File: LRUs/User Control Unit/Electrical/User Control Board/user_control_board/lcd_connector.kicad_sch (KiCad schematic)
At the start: 1 part

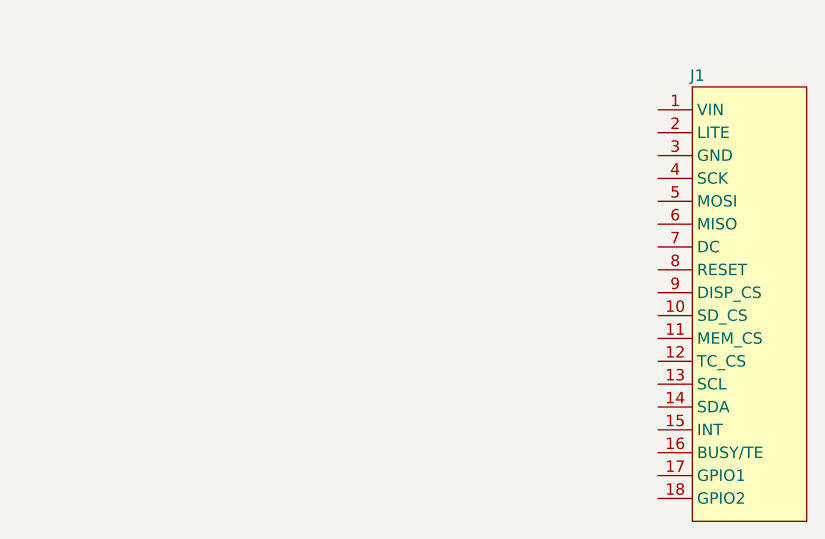
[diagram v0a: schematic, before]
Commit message: PICO partial wiring to -> (EYESPI, RFM transceiver).  Mosfet partially wired.
Don't know how to do the SD card XD.
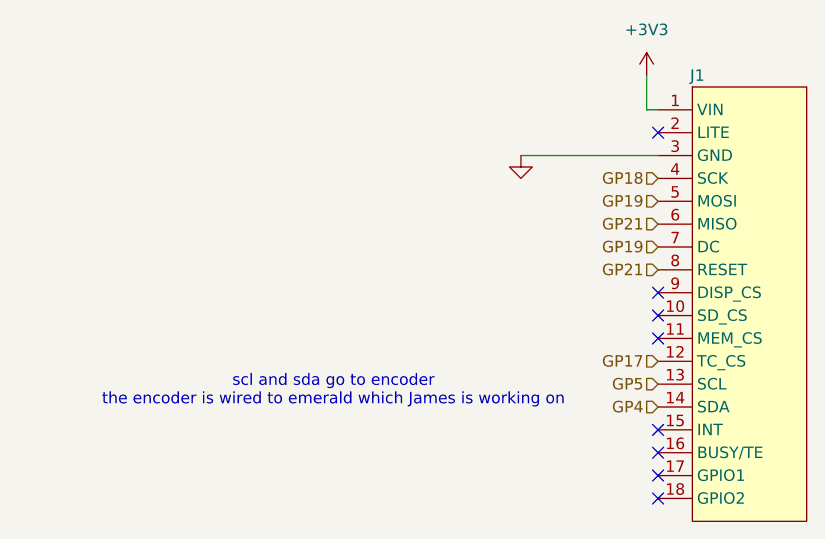
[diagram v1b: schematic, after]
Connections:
- net +3V3: now reaches J1.1 (VIN)
- net GP17: now reaches J1.12 (TC_CS)
- net GP5: now reaches J1.13 (SCL)
- net GP4: now reaches J1.14 (SDA)
- net GND: now reaches J1.3 (GND)
- net GP18: now reaches J1.4 (SCK)
- net GP19: now reaches J1.5 (MOSI)
- net GP19: now also J1.7 (DC)
- net GP21: now reaches J1.6 (MISO)
- net GP21: now also J1.8 (RESET)
- no-connect marks 0 -> 8
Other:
- note added: "scl and sda go to encoder the encoder is wired to emerald which James is working on"

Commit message: need to run DCR
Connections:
- net GP19: no longer J1.7 (DC)
- net GP21: no longer J1.6 (MISO)
- new net GP16: J1.6 (MISO)
- new net GP20: J1.7 (DC)
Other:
- note removed: "scl and sda go to encoder the encoder is wired to emerald which James is working on"
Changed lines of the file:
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@@
 	(generator_version "10.0")
 	(paper "A4")
-	(text "scl and sda go to encoder\nthe encoder is wired to emerald which James is working on"
-		(exclude_from_sim no)
-		(at 162.052 106.172 0)
-		(effects
-			(font
-				(size 1.27 1.27)
-			)
-		)
-	)
 	(no_connect
 		(at 198.12 113.03)
@@
 		)
 	)
-	(hierarchical_label "GP21"
+	(global_label "GP20"
+		(shape input)
+		(at 198.12 90.17 180)
+		(fields_autoplaced yes)
+		(effects
+			(font
+				(size 1.27 1.27)
+			)
+			(justify right)
+		)
+		(property "Intersheetrefs" "${INTERSHEET_REFS}"
+			(at 190.1758 90.17 0)
+			(hide yes)
+			(show_name no)
+			(do_not_autoplace no)
+			(effects
+				(font
+					(size 1.27 1.27)
+				)
+				(justify right)
+			)
+		)
+	)
+	(global_label "GP5"
+		(shape input)
+		(at 198.12 105.41 180)
+		(fields_autoplaced yes)
+		(effects
+			(font
+				(size 1.27 1.27)
+			)
+			(justify right)
+		)
+		(property "Intersheetrefs" "${INTERSHEET_REFS}"
+			(at 191.3853 105.41 0)
+			(hide yes)
+			(show_name no)
+			(do_not_autoplace no)
+			(effects
+				(font
+					(size 1.27 1.27)
+				)
+				(justify right)
+			)
+		)
+	)
+	(global_label "GP18"
+		(shape input)
+		(at 198.12 82.55 180)
+		(fields_autoplaced yes)
+		(effects
+			(font
+				(size 1.27 1.27)
+			)
+			(justify right)
+		)
+		(property "Intersheetrefs" "${INTERSHEET_REFS}"
+			(at 190.1758 82.55 0)
+			(hide yes)
+			(show_name no)
+			(do_not_autoplace no)
+			(effects
+				(font
+					(size 1.27 1.27)
+				)
+				(justify right)
+			)
+		)
+	)
+	(global_label "GP21"
+		(shape input)
+		(at 198.12 92.71 180)
+		(fields_autoplaced yes)
+		(effects
+			(font
+				(size 1.27 1.27)
+			)
+			(justify right)
+		)
+		(property "Intersheetrefs" "${INTERSHEET_REFS}"
+			(at 190.1758 92.71 0)
+			(hide yes)
+			(show_name no)
+			(do_not_autoplace no)
+			(effects
+				(font
+					(size 1.27 1.27)
+				)
+				(justify right)
+			)
+		)
+	)
+	(global_label "GP4"
+		(shape input)
+		(at 198.12 107.95 180)
+		(fields_autoplaced yes)
+		(effects
+			(font
+				(size 1.27 1.27)
+			)
+			(justify right)
+		)
+		(property "Intersheetrefs" "${INTERSHEET_REFS}"
+			(at 191.3853 107.95 0)
+			(hide yes)
+			(show_name no)
+			(do_not_autoplace no)
+			(effects
+				(font
+					(size 1.27 1.27)
+				)
+				(justify right)
+			)
+		)
+	)
+	(global_label "GP17"
+		(shape input)
+		(at 198.12 102.87 180)
+		(fields_autoplaced yes)
+		(effects
+			(font
+				(size 1.27 1.27)
+			)
+			(justify right)
+		)
+		(property "Intersheetrefs" "${INTERSHEET_REFS}"
+			(at 190.1758 102.87 0)
+			(hide yes)
+			(show_name no)
+			(do_not_autoplace no)
+			(effects
+				(font
+					(size 1.27 1.27)
+				)
+				(justify right)
+			)
+		)
+	)
+	(global_label "GP16"
 		(shape input)
 		(at 198.12 87.63 180)
-		(effects
-			(font
-				(size 1.27 1.27)
-			)
-			(justify right)
-		)
-	)
-	(hierarchical_label "GP21"
-		(shape input)
-		(at 198.12 92.71 180)
-		(effects
-			(font
-				(size 1.27 1.27)
-			)
-			(justify right)
-		)
-	)
-	(hierarchical_label "GP19"
+		(fields_autoplaced yes)
+		(effects
+			(font
+				(size 1.27 1.27)
+			)
+			(justify right)
+		)
+		(property "Intersheetrefs" "${INTERSHEET_REFS}"
+			(at 190.1758 87.63 0)
+			(hide yes)
+			(show_name no)
+			(do_not_autoplace no)
+			(effects
+				(font
+					(size 1.27 1.27)
+				)
+				(justify right)
+			)
+		)
+	)
+	(global_label "GP19"
 		(shape input)
 		(at 198.12 85.09 180)
-		(effects
-			(font
-				(size 1.27 1.27)
-			)
-			(justify right)
-		)
-	)
-	(hierarchical_label "GP19"
-		(shape input)
-		(at 198.12 90.17 180)
-		(effects
-			(font
-				(size 1.27 1.27)
-			)
-			(justify right)
-		)
-	)
-	(hierarchical_label "GP5"
-		(shape input)
-		(at 198.12 105.41 180)
-		(effects
-			(font
-				(size 1.27 1.27)
-			)
-			(justify right)
-		)
-	)
-	(hierarchical_label "GP18"
-		(shape input)
-		(at 198.12 82.55 180)
-		(effects
-			(font
-				(size 1.27 1.27)
-			)
-			(justify right)
-		)
-	)
-	(hierarchical_label "GP4"
-		(shape input)
-		(at 198.12 107.95 180)
-		(effects
-			(font
-				(size 1.27 1.27)
-			)
-			(justify right)
-		)
-	)
-	(hierarchical_label "GP17"
-		(shape input)
-		(at 198.12 102.87 180)
-		(effects
-			(font
-				(size 1.27 1.27)
-			)
-			(justify right)
-		)
-	)
+		(fields_autoplaced yes)
+		(effects
+			(font
+				(size 1.27 1.27)
+			)
+			(justify right)
+		)
+		(property "Intersheetrefs" "${INTERSHEET_REFS}"
+			(at 190.1758 85.09 0)
+			(hide yes)
+			(show_name no)
+			(do_not_autoplace no)
+			(effects
+				(font
+					(size 1.27 1.27)
+				)
+				(justify right)
+			)
+		)
+	)

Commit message: connectors and 5v buck partially done
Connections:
- net GP16 renamed RADIO_CS
- net GP17 renamed LCD_CS
- net GP18 renamed SCK
- net GP19 renamed MOSI
- net GP20 renamed LCD_DC
- net GP21 renamed LCD_RESET
- net GP4 renamed I2C0_SDA
- net GP5 renamed I2C0_SCL
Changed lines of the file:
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@@
 		)
 	)
-	(global_label "GP20"
+	(global_label "LCD_DC"
 		(shape input)
 		(at 198.12 90.17 180)
@@
 		)
 		(property "Intersheetrefs" "${INTERSHEET_REFS}"
-			(at 190.1758 90.17 0)
-			(hide yes)
-			(show_name no)
-			(do_not_autoplace no)
-			(effects
-				(font
-					(size 1.27 1.27)
-				)
-				(justify right)
-			)
-		)
-	)
-	(global_label "GP5"
+			(at 188.0591 90.17 0)
+			(hide yes)
+			(show_name no)
+			(do_not_autoplace no)
+			(effects
+				(font
+					(size 1.27 1.27)
+				)
+				(justify right)
+			)
+		)
+	)
+	(global_label "I2C0_SDA"
+		(shape input)
+		(at 198.12 107.95 180)
+		(fields_autoplaced yes)
+		(effects
+			(font
+				(size 1.27 1.27)
+			)
+			(justify right)
+		)
+		(property "Intersheetrefs" "${INTERSHEET_REFS}"
+			(at 186.3053 107.95 0)
+			(hide yes)
+			(show_name no)
+			(do_not_autoplace no)
+			(effects
+				(font
+					(size 1.27 1.27)
+				)
+				(justify right)
+			)
+		)
+	)
+	(global_label "SCK"
+		(shape input)
+		(at 198.12 82.55 180)
+		(fields_autoplaced yes)
+		(effects
+			(font
+				(size 1.27 1.27)
+			)
+			(justify right)
+		)
+		(property "Intersheetrefs" "${INTERSHEET_REFS}"
+			(at 191.3853 82.55 0)
+			(hide yes)
+			(show_name no)
+			(do_not_autoplace no)
+			(effects
+				(font
+					(size 1.27 1.27)
+				)
+				(justify right)
+			)
+		)
+	)
+	(global_label "LCD_RESET"
+		(shape input)
+		(at 198.12 92.71 180)
+		(fields_autoplaced yes)
+		(effects
+			(font
+				(size 1.27 1.27)
+			)
+			(justify right)
+		)
+		(property "Intersheetrefs" "${INTERSHEET_REFS}"
+			(at 184.854 92.71 0)
+			(hide yes)
+			(show_name no)
+			(do_not_autoplace no)
+			(effects
+				(font
+					(size 1.27 1.27)
+				)
+				(justify right)
+			)
+		)
+	)
+	(global_label "LCD_CS"
+		(shape input)
+		(at 198.12 102.87 180)
+		(fields_autoplaced yes)
+		(effects
+			(font
+				(size 1.27 1.27)
+			)
+			(justify right)
+		)
+		(property "Intersheetrefs" "${INTERSHEET_REFS}"
+			(at 188.1196 102.87 0)
+			(hide yes)
+			(show_name no)
+			(do_not_autoplace no)
+			(effects
+				(font
+					(size 1.27 1.27)
+				)
+				(justify right)
+			)
+		)
+	)
+	(global_label "RADIO_CS"
+		(shape input)
+		(at 198.12 87.63 180)
+		(fields_autoplaced yes)
+		(effects
+			(font
+				(size 1.27 1.27)
+			)
+			(justify right)
+		)
+		(property "Intersheetrefs" "${INTERSHEET_REFS}"
+			(at 186.1238 87.63 0)
+			(hide yes)
+			(show_name no)
+			(do_not_autoplace no)
+			(effects
+				(font
+					(size 1.27 1.27)
+				)
+				(justify right)
+			)
+		)
+	)
+	(global_label "I2C0_SCL"
 		(shape input)
 		(at 198.12 105.41 180)
@@
 		)
 		(property "Intersheetrefs" "${INTERSHEET_REFS}"
-			(at 191.3853 105.41 0)
-			(hide yes)
-			(show_name no)
-			(do_not_autoplace no)
-			(effects
-				(font
-					(size 1.27 1.27)
-				)
-				(justify right)
-			)
-		)
-	)
-	(global_label "GP18"
-		(shape input)
-		(at 198.12 82.55 180)
-		(fields_autoplaced yes)
-		(effects
-			(font
-				(size 1.27 1.27)
-			)
-			(justify right)
-		)
-		(property "Intersheetrefs" "${INTERSHEET_REFS}"
-			(at 190.1758 82.55 0)
-			(hide yes)
-			(show_name no)
-			(do_not_autoplace no)
-			(effects
-				(font
-					(size 1.27 1.27)
-				)
-				(justify right)
-			)
-		)
-	)
-	(global_label "GP21"
-		(shape input)
-		(at 198.12 92.71 180)
-		(fields_autoplaced yes)
-		(effects
-			(font
-				(size 1.27 1.27)
-			)
-			(justify right)
-		)
-		(property "Intersheetrefs" "${INTERSHEET_REFS}"
-			(at 190.1758 92.71 0)
-			(hide yes)
-			(show_name no)
-			(do_not_autoplace no)
-			(effects
-				(font
-					(size 1.27 1.27)
-				)
-				(justify right)
-			)
-		)
-	)
-	(global_label "GP4"
-		(shape input)
-		(at 198.12 107.95 180)
-		(fields_autoplaced yes)
-		(effects
-			(font
-				(size 1.27 1.27)
-			)
-			(justify right)
-		)
-		(property "Intersheetrefs" "${INTERSHEET_REFS}"
-			(at 191.3853 107.95 0)
-			(hide yes)
-			(show_name no)
-			(do_not_autoplace no)
-			(effects
-				(font
-					(size 1.27 1.27)
-				)
-				(justify right)
-			)
-		)
-	)
-	(global_label "GP17"
-		(shape input)
-		(at 198.12 102.87 180)
-		(fields_autoplaced yes)
-		(effects
-			(font
-				(size 1.27 1.27)
-			)
-			(justify right)
-		)
-		(property "Intersheetrefs" "${INTERSHEET_REFS}"
-			(at 190.1758 102.87 0)
-			(hide yes)
-			(show_name no)
-			(do_not_autoplace no)
-			(effects
-				(font
-					(size 1.27 1.27)
-				)
-				(justify right)
-			)
-		)
-	)
-	(global_label "GP16"
-		(shape input)
-		(at 198.12 87.63 180)
-		(fields_autoplaced yes)
-		(effects
-			(font
-				(size 1.27 1.27)
-			)
-			(justify right)
-		)
-		(property "Intersheetrefs" "${INTERSHEET_REFS}"
-			(at 190.1758 87.63 0)
-			(hide yes)
-			(show_name no)
-			(do_not_autoplace no)
-			(effects
-				(font
-					(size 1.27 1.27)
-				)
-				(justify right)
-			)
-		)
-	)
-	(global_label "GP19"
+			(at 186.3658 105.41 0)
+			(hide yes)
+			(show_name no)
+			(do_not_autoplace no)
+			(effects
+				(font
+					(size 1.27 1.27)
+				)
+				(justify right)
+			)
+		)
+	)
+	(global_label "MOSI"
 		(shape input)
 		(at 198.12 85.09 180)
@@
 		)
 		(property "Intersheetrefs" "${INTERSHEET_REFS}"
-			(at 190.1758 85.09 0)
+			(at 190.5386 85.09 0)
 			(hide yes)
 			(show_name no)
@@
 		(dnp no)
 		(fields_autoplaced yes)
-		(property "Reference" "#PWR017"
+		(property "Reference" "#PWR05"
 			(at 196.85 74.93 0)
 			(hide yes)
@@
 			(project "user_control_board"
 				(path "/bc27608c-d267-4607-a115-e0984dc927e7"
-					(reference "#PWR017")
+					(reference "#PWR05")
 					(unit 1)
 				)
@@
 		(dnp no)
 		(fields_autoplaced yes)
-		(property "Reference" "#PWR018"
+		(property "Reference" "#PWR04"
 			(at 182.88 86.36 0)
 			(hide yes)
@@
 			(project "user_control_board"
 				(path "/bc27608c-d267-4607-a115-e0984dc927e7"
-					(reference "#PWR018")
+					(reference "#PWR04")
 					(unit 1)
 				)
